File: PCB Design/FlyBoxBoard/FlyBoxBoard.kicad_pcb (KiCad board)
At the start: 2 copper layers, 148.6 x 119.4 mm, 43 parts, among them J1 5V in, J10 RED, J11 GREEN, J12 WHITE, J13 INFRARED, J14 LCD Screen, J15 SD card reader, J16 5K Ohms, J17 5K Ohms, J18 ESP 32 Left Side extra pinouts, J19 ESP 32 Left Side extra pinouts, J2 12V in, J20 Transistor, J21 Logic Level LV pins, J22 Potentiometer, J23 Logic Level Left Side LV, J25 ESP 32 Right Side extra pinou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, J26 BuckPuck IR, J27 Logic Level Right Side HV, J28 Logic Level HV pins, J29 5K Ohms, J3 ESP 32 Left Side, J30 5K Ohms, J31 5K Ohms, J32 5K Ohms, J33 5K Ohms, J34 5K Ohms, J35 Transistor, J36 Transistor, J37 Transistor, J38 BuckPuck White, J39 BuckPuck Green, J4 Real Time Controller, J40 BuckPuck Red, J5 ESP 32 Right Side, J6 Rotary Knob, J9 FANS

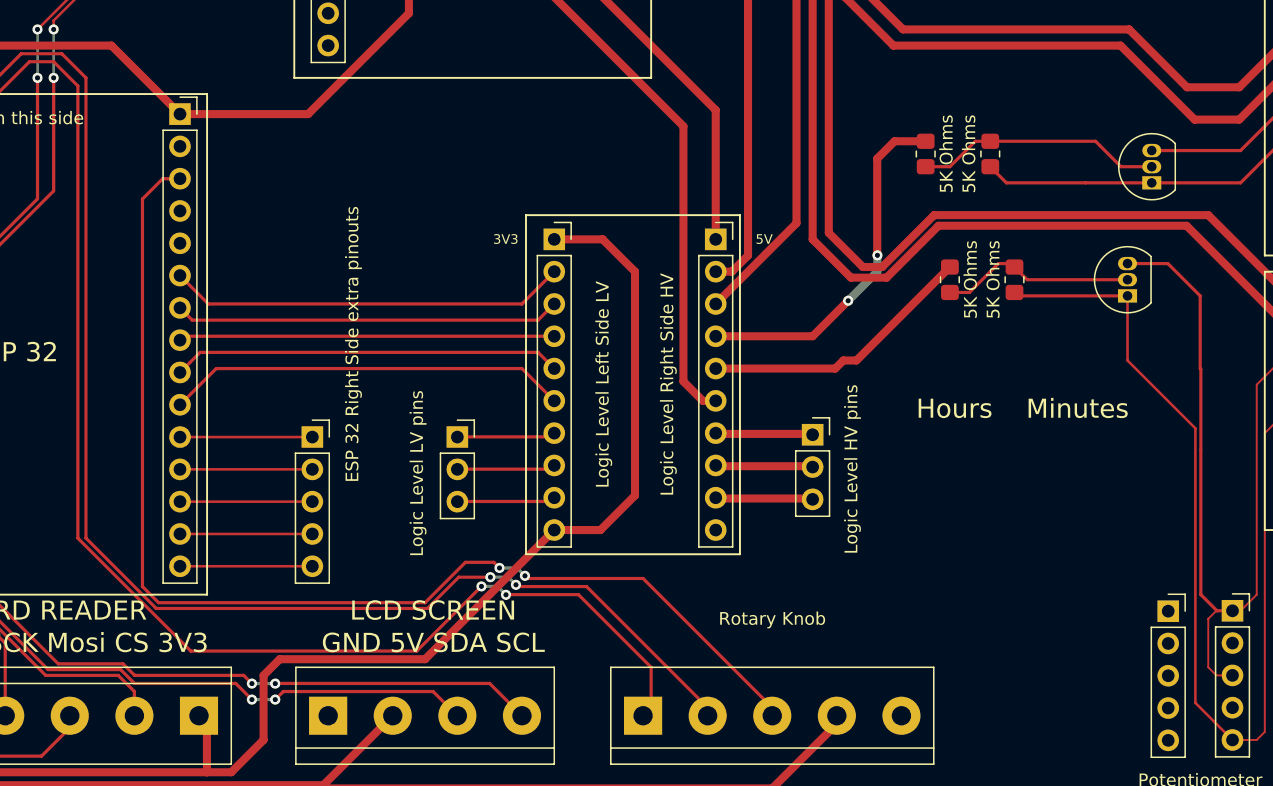
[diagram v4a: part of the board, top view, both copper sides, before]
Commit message: Finished V2 PCBs with rounded edges
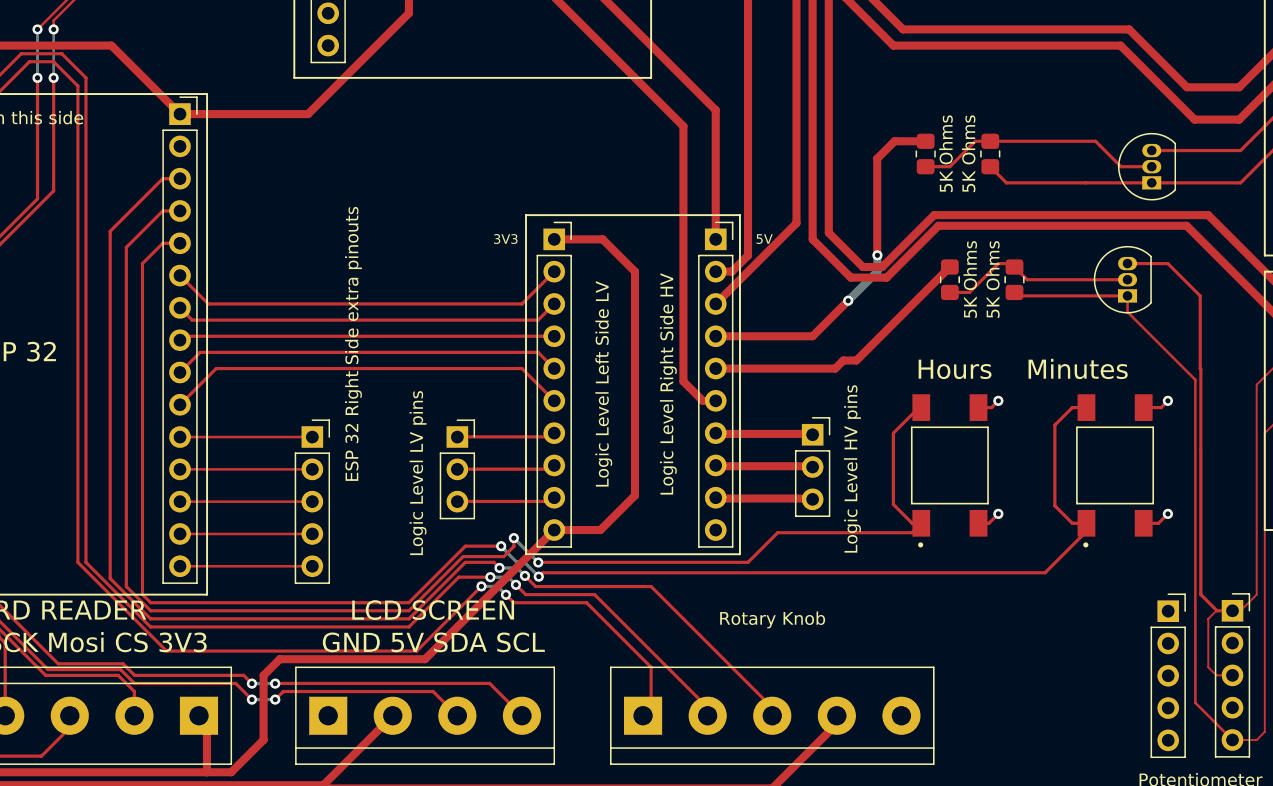
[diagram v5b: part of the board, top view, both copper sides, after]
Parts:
- added S1: Hours, SnapEDA-Library:SW_1571563-2, F.Cu at (117.5, 109.2)
- added S2: Minutes, SnapEDA-Library:SW_1571563-2, F.Cu at (130.5, 109.2)
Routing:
- net /D14: track 0.00 -> 121.6 mm, vias 0 -> 2
- net /D12: track 0.00 -> 111.7 mm, vias 0 -> 2
- net /GND: track 0.00 -> 7.98 mm, vias 4 -> 8
- net /D13: track 90.8 -> 95.1 mm
- net /D4: track 120.5 -> 122.9 mm
- net /D15: track 115.1 -> 116.2 mm

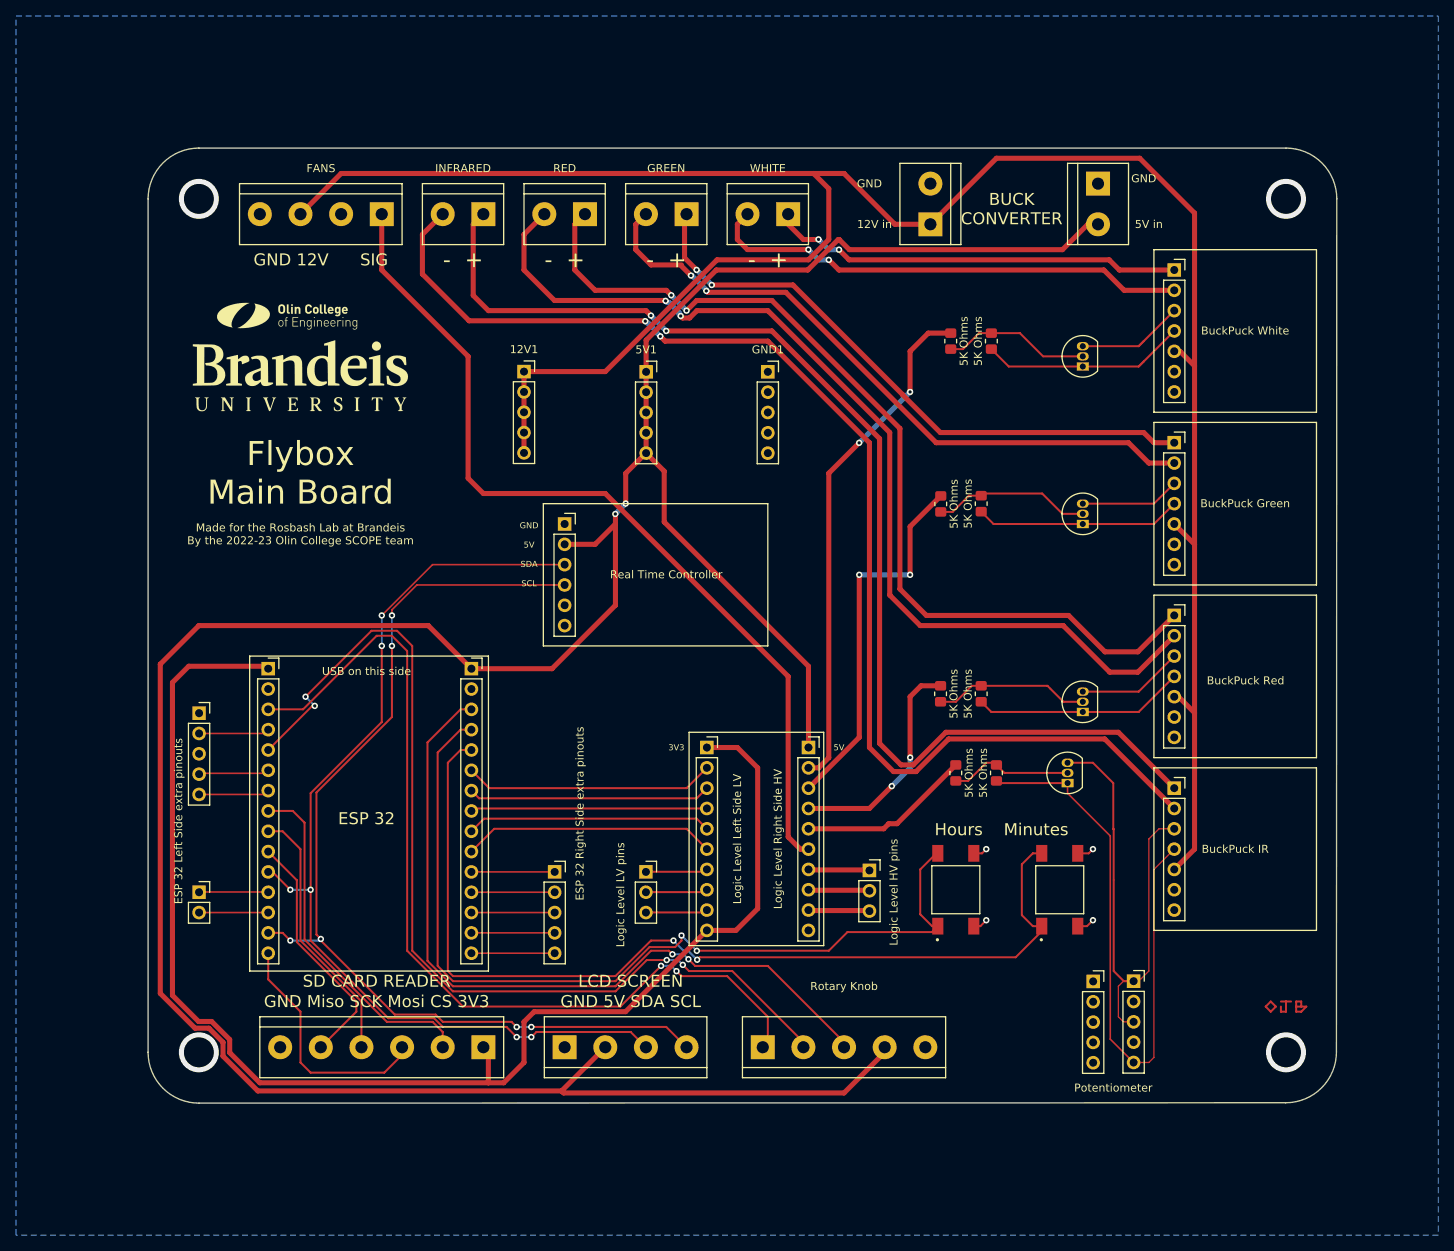
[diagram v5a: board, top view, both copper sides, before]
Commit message: Zachary first pass on V2 of FlyBoxBoard
Not done yet, still need to look at/think about more.
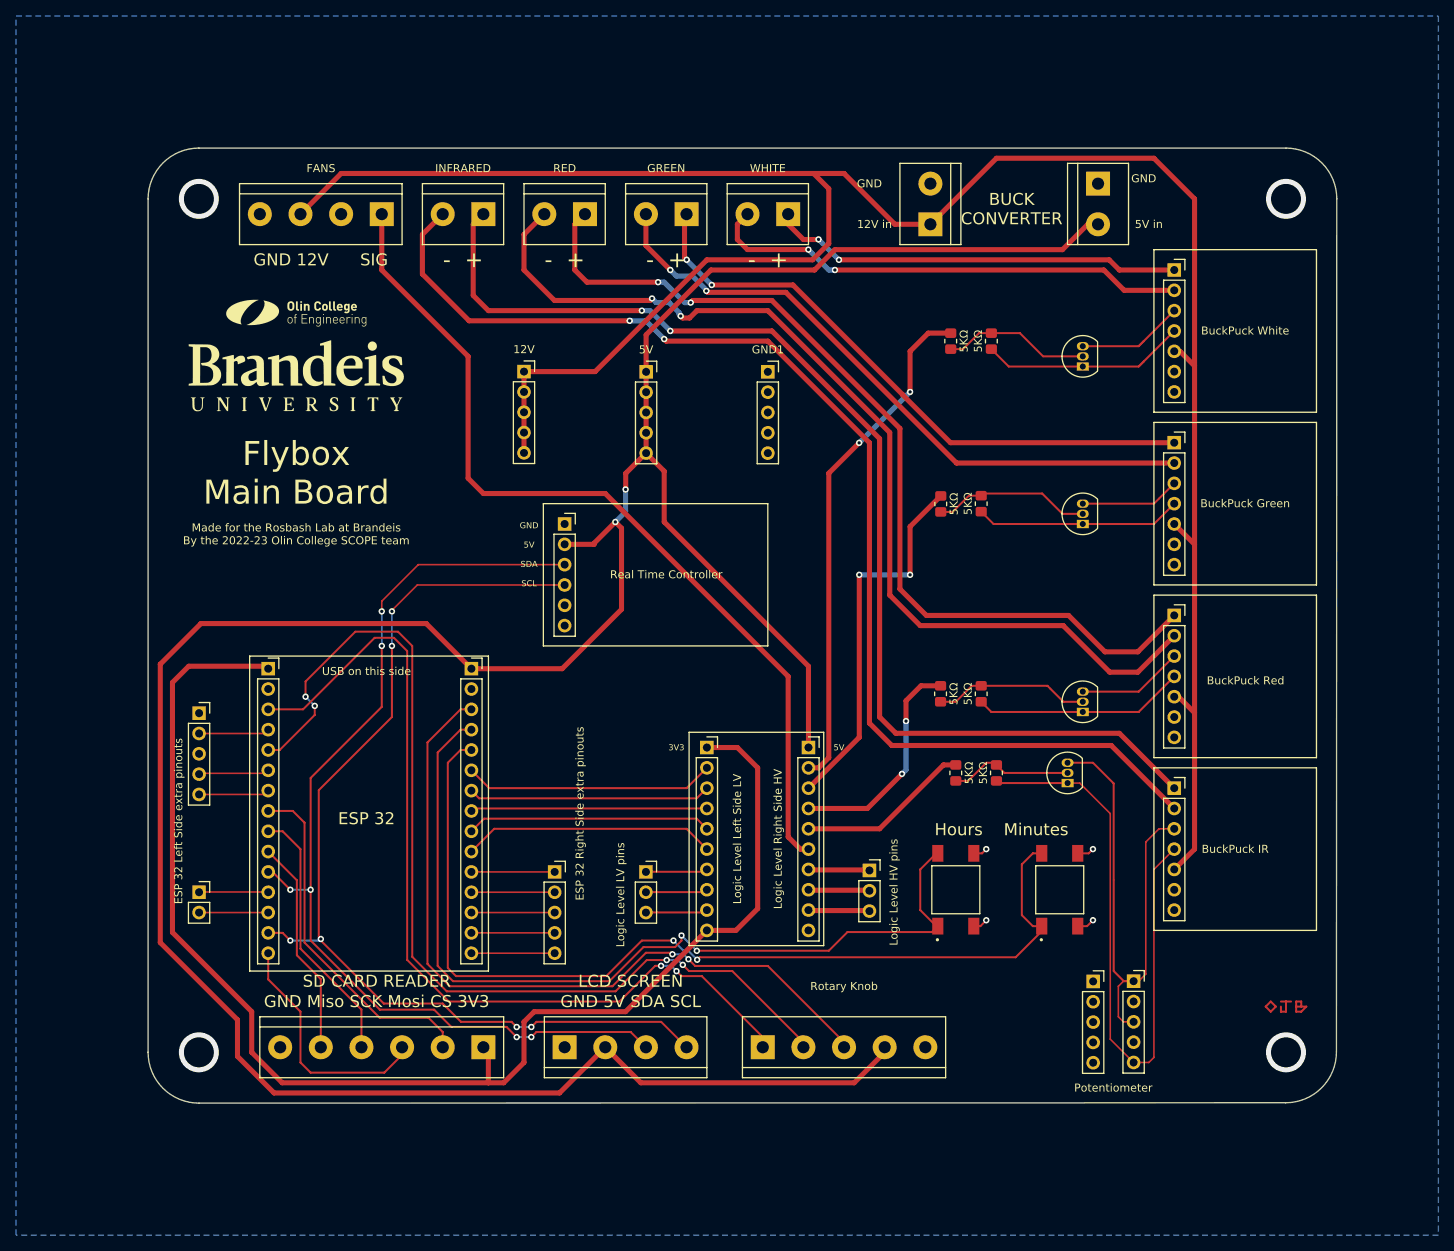
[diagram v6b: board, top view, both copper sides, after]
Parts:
- J16, J17, J29, J30, J31, J32, J33, J34: value 5K Ohms -> 5KΩ
- moved G*** 1.20 mm to (34.8, 37.1)
- moved G*** 0.52 mm to (35.0, 45.1)
- renumbered 12V1 to 12V, 5V1 to 5V
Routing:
- net /IR LED+: track 149.5 -> 144.2 mm
- net /IR LED-: track 156.0 -> 150.7 mm
- net /5V: track 363.6 -> 358.6 mm
- net /D19: track 30.9 -> 27.2 mm
- net /3V3: track 172.4 -> 169.8 mm
- net /D15: track 116.2 -> 113.8 mm
- net /D4: track 122.9 -> 125.0 mm
- net /G LED-: track 83.3 -> 81.3 mm
- net /12V: track 280.3 -> 281.6 mm
- net /D21: track 124.0 -> 125.0 mm
- net Net-(J16-Pad2): track 77.2 -> 78.1 mm
- net /R LED+: track 116.9 -> 116.1 mm
